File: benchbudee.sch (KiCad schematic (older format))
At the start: 0 parts

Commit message: Module 3 Unit 10
Revisiting The Current/Fan Module
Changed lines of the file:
@@
 F6 "Relay+" O R 4000 6500 60
 F7 "Relay-" O R 4000 6700 60
-F8 "Fan_En_N" O R 4000 4200 60
-F9 "Current_Measure" I R 4000 4400 60
-F10 "V+ADJ_MON" I R 4000 3200 60
-F11 "V-ADJ_MON" I R 4000 3300 60
-F12 "LED_EN_PWM" O R 4000 5300 60
-F13 "DAC_CS_N" O R 4000 4100 60
-F14 "ADC_CS_N" O R 4000 4000 60
+F8 "Current_Measure" I R 4000 4400 60
+F9 "V+ADJ_MON" I R 4000 3200 60
+F10 "V-ADJ_MON" I R 4000 3300 60
+F11 "LED_EN_PWM" O R 4000 5300 60
+F12 "DAC_CS_N" O R 4000 4100 60
+F13 "ADC_CS_N" O R 4000 4000 60
+F14 "FAN_PWM" O R 4000 4200 60
+F15 "FAN_MODE" I R 4000 4500 60
 $EndSheet
 $Sheet
@@
 F7 "Tach_In" I R 9300 3600 60
 F8 "Tach_Meas" O L 6600 4300 60
-F9 "Fan_En_N" I L 6600 4200 60
-F10 "Current_Measure" O L 6600 4400 60
-F11 "Fan_Out-" O R 9300 3400 60
+F9 "Current_Measure" O L 6600 4400 60
+F10 "Fan_Out-" O R 9300 3400 60
+F11 "FAN_PWM" I L 6600 4200 60
+F12 "FAN_MODE" I L 6600 4500 60
 $EndSheet
 $Sheet
@@
 Wire Wire Line
 	6600 6700 4000 6700
+Wire Wire Line
+	4000 4500 6600 4500
 $EndSCHEMATC

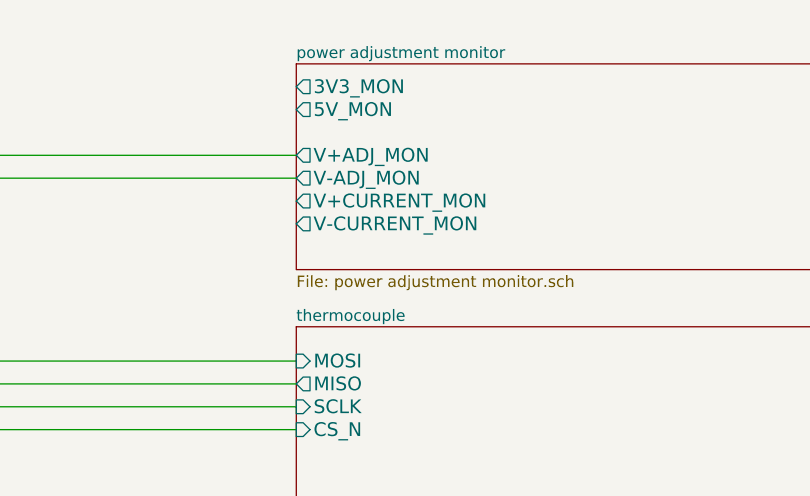
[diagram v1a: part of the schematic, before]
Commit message: Module 3 Unit 15
Choosing Components For The Power Control, Conditioning, Monitoring
Module
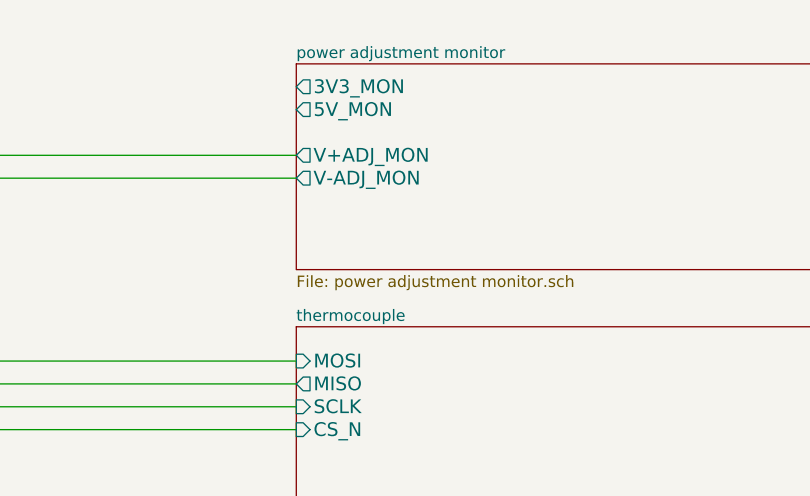
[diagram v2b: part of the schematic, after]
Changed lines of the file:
@@
 Sheet 1 9
 Title ""
-Date "16 feb 2014"
+Date "22 feb 2014"
 Rev ""
 Comp ""
@@
 F4 "V+ADJ_MON" O L 6600 1200 60
 F5 "V-ADJ_MON" O L 6600 1300 60
-F6 "V+CURRENT_MON" O L 6600 1400 60
-F7 "V-CURRENT_MON" O L 6600 1500 60
 F8 "V+ADJ" O R 9300 1150 60
 F9 "V-ADJ" O R 9300 1350 60
